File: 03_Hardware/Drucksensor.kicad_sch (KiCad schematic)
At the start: 100 parts, among them J110 DS18B20, J111 Conn_01x06_Male, Q1 BC817, SW103 SW_DIP_x08, U103 ATmega8A-A, U104 REF3040, U105 74HC165, U107 SN75176AD, U108 CAT24M01W, Y101 16MHz

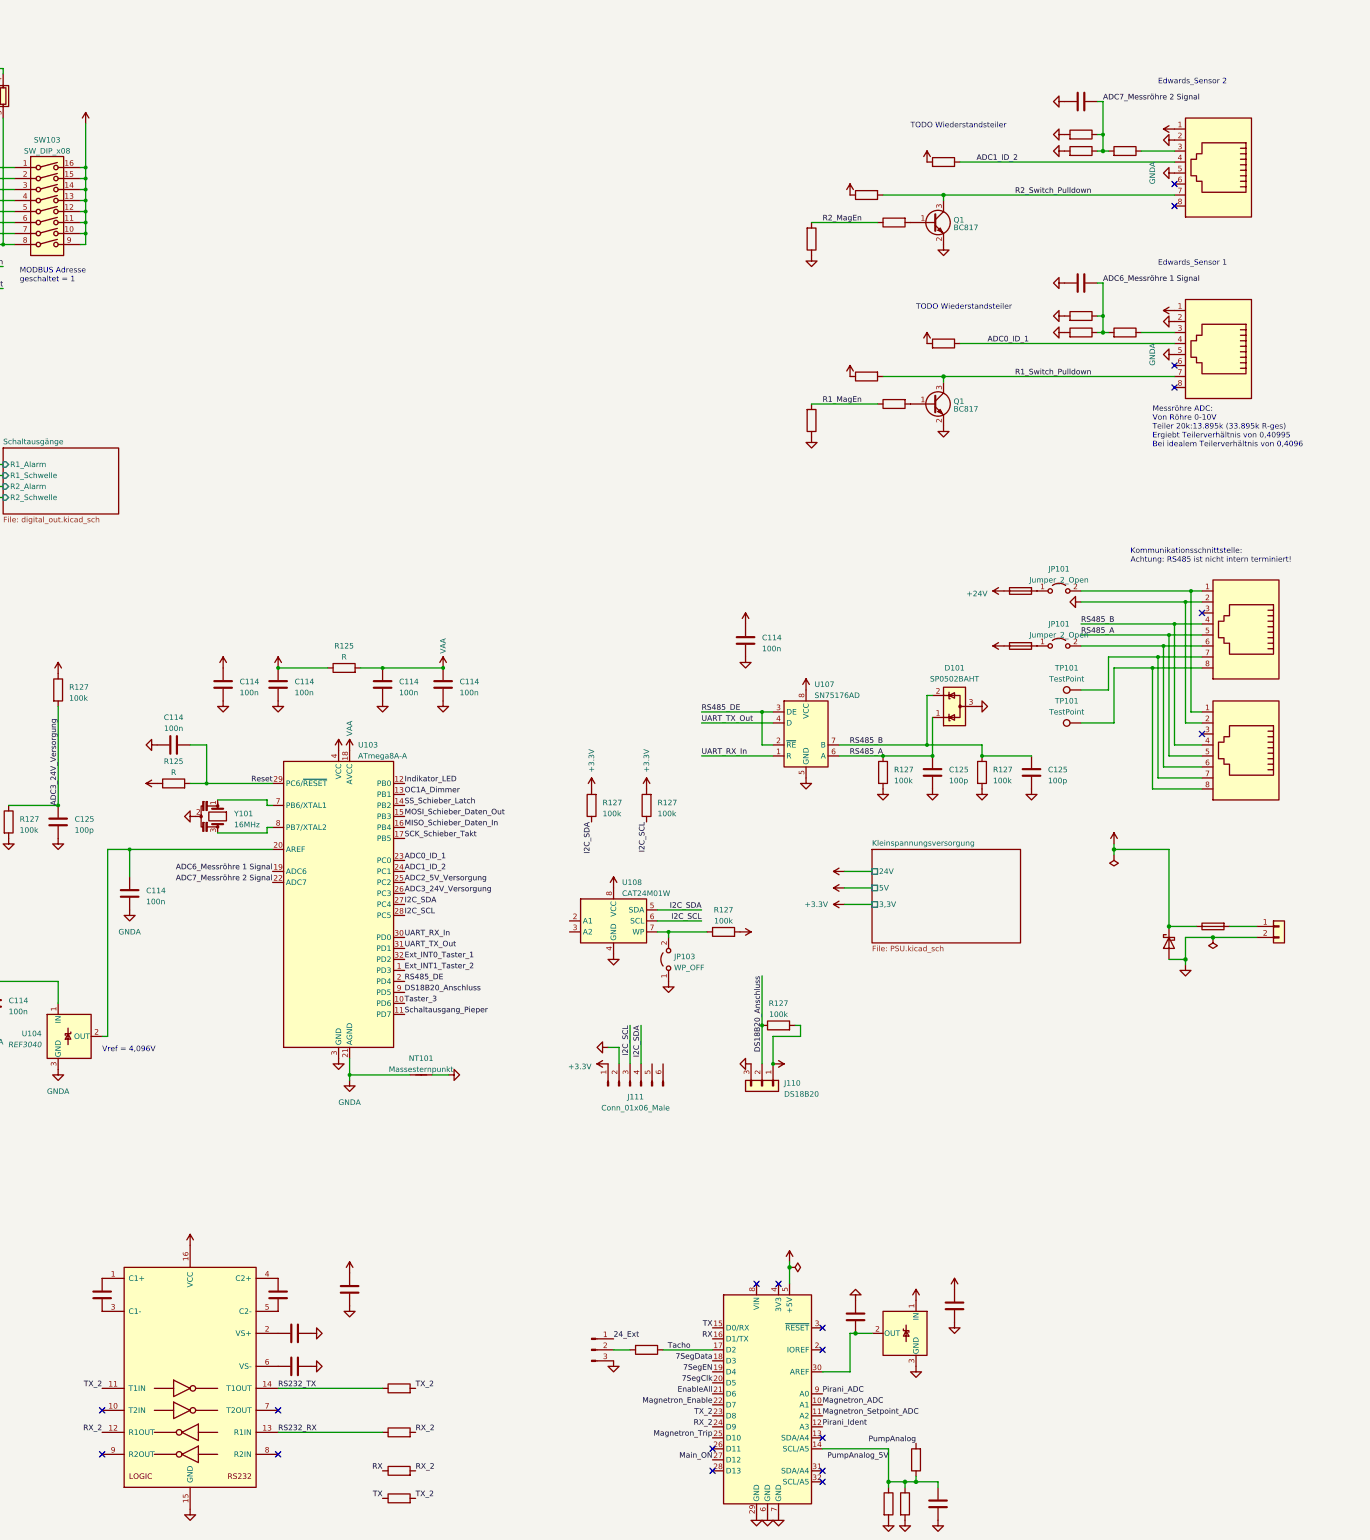
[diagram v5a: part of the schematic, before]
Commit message: RJ45-Anschlüsse überarbeitet
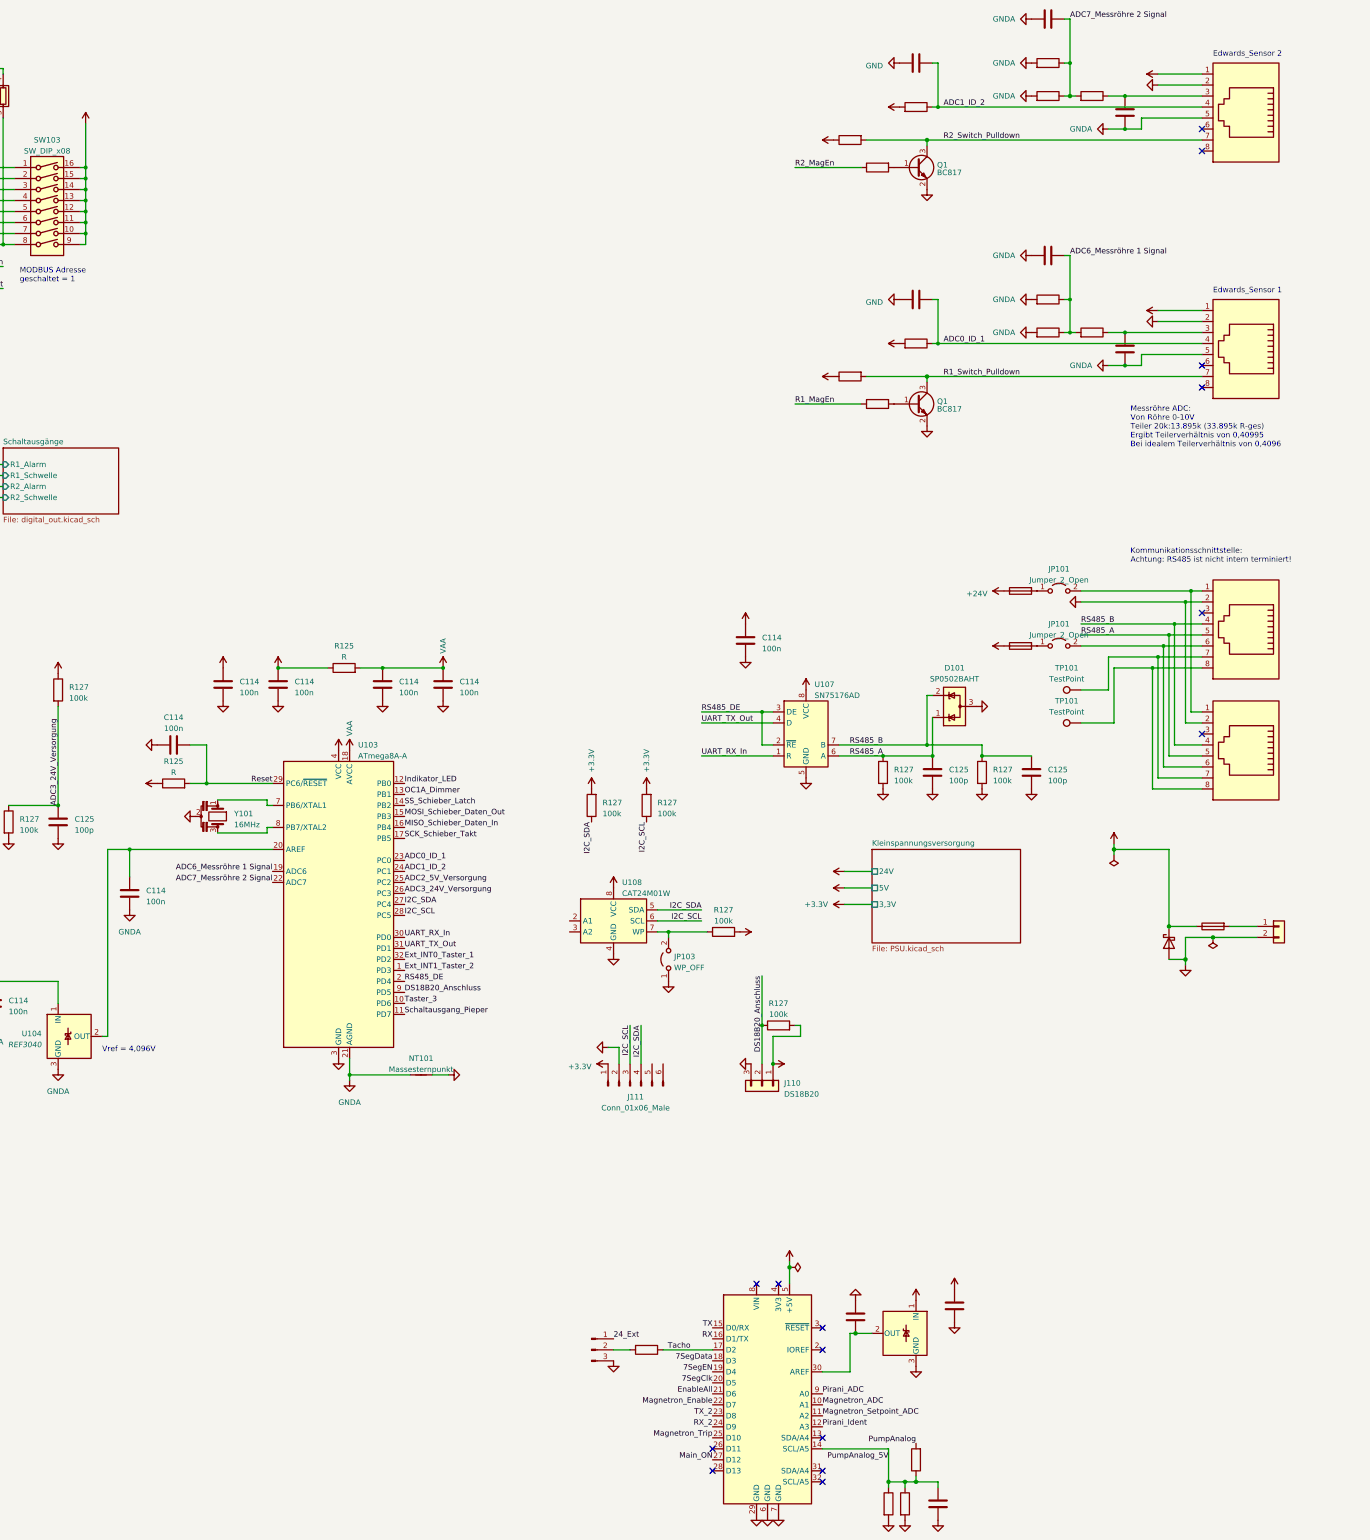
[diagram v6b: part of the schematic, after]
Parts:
- removed ? (x6): (no value), symbol Device:R
- removed ? (x5): (no value), symbol Device:C
- removed ?: (no value), symbol Interface_UART:MAX232
- added ? (x4): (no value), symbol Device:C
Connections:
- net ADC0_ID_1: now also ?.1
- net ADC1_ID_2: now also ?.1
- net GND: now also ?.2, ?.2; no longer ?.2, ?.2, ?.2, ?.2, ?.2, ?.2
- net GNDA: now also ?.2, ?.2, ?.2, ?.2, ?.2, ?.2, ?.2, ?.2
- net at ?.1, ?.3: now also ?.1 (x2)
- no-connect marks 23 -> 19
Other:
- note added: "Messröhre ADC: Von Röhre 0-10V Teiler 20k:13.895k (33.895k R-ges) Ergibt Teilerverhältnis von 0,40995 Bei idealem Teilerverhältnis von 0,4096"
- note removed: "Messröhre ADC: Von Röhre 0-10V Teiler 20k:13.895k (33.895k R-ges) Ergiebt Teilerverhältnis von 0,40995 Bei idealem Teilerverhältnis von 0,4096"
- note removed: "TODO Wiederstandsteiler"
- title: Vakkumanzeige für zwei aktive Vakuumsensoren -> Anzeigegerät für zwei aktive Vakuumsensoren
- moved on the sheet: Q1

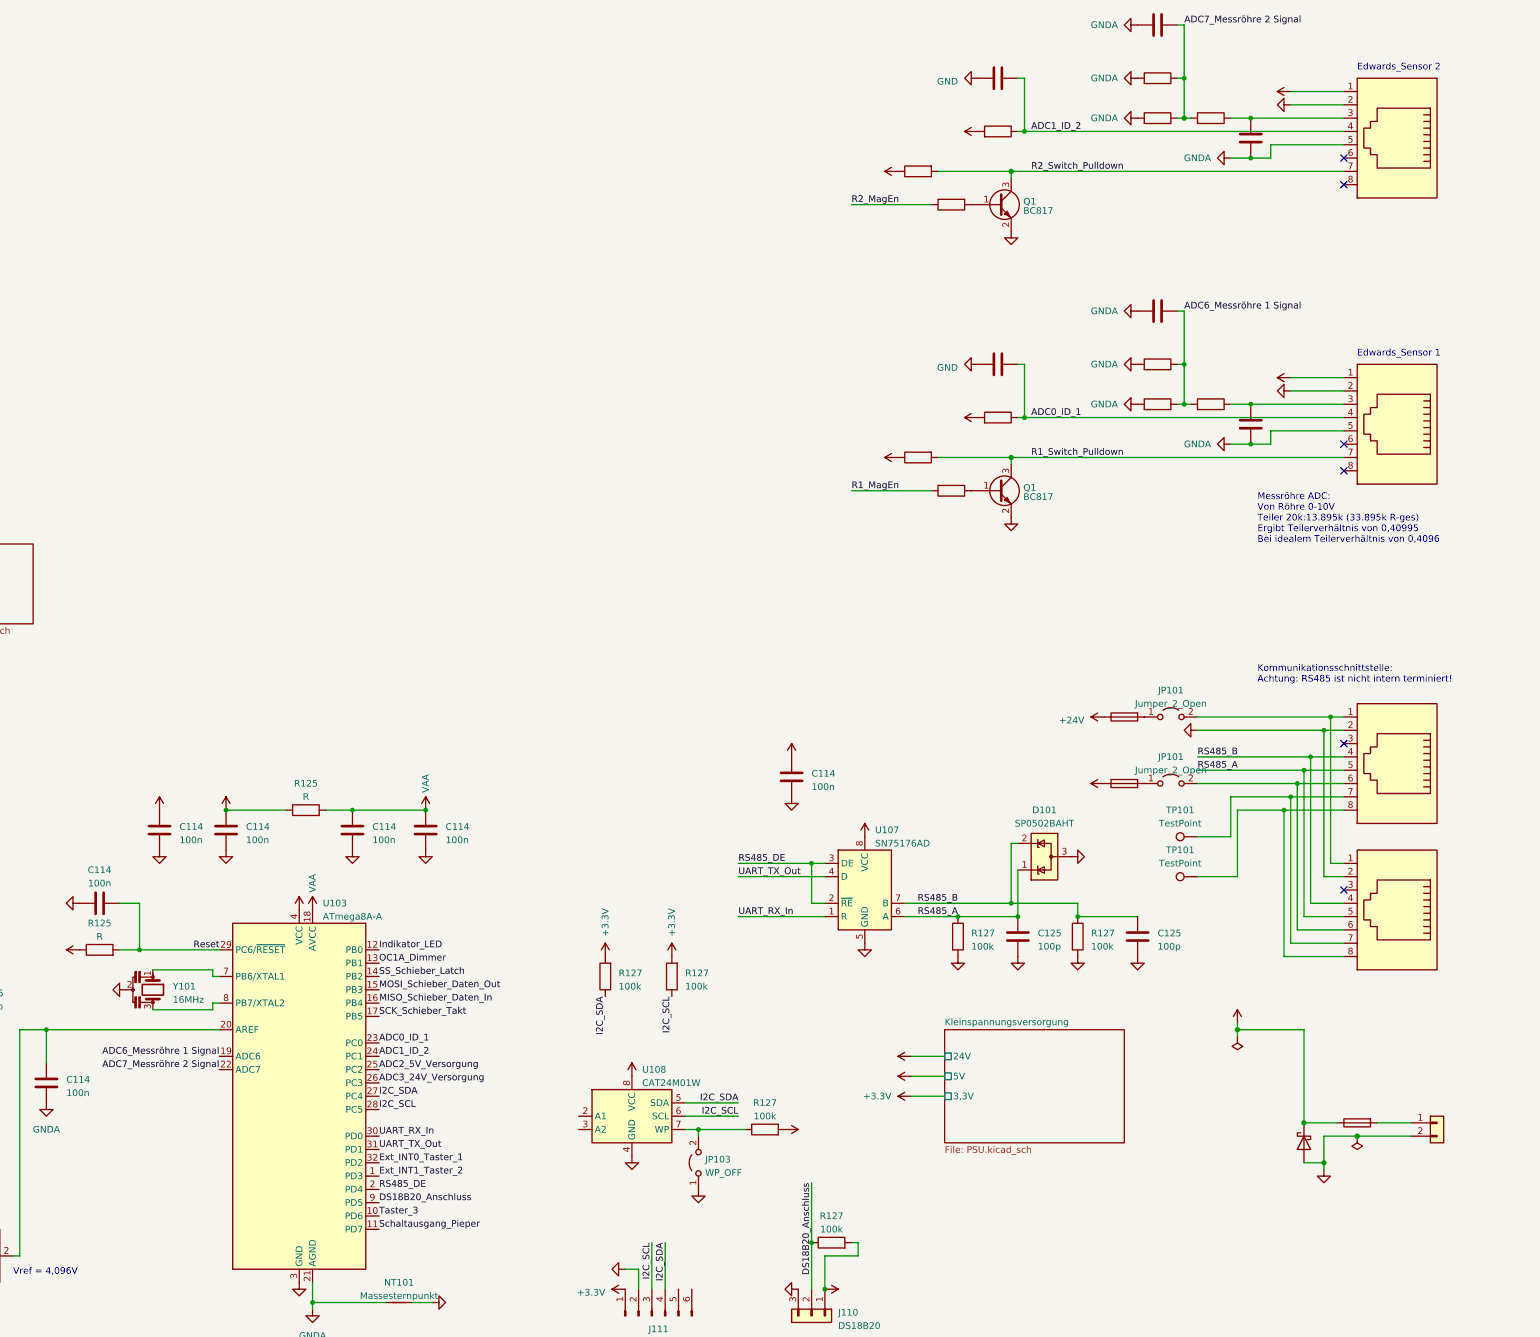
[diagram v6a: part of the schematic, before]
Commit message: TVS Dioden für Signal und DS18b20 hinzugefügt
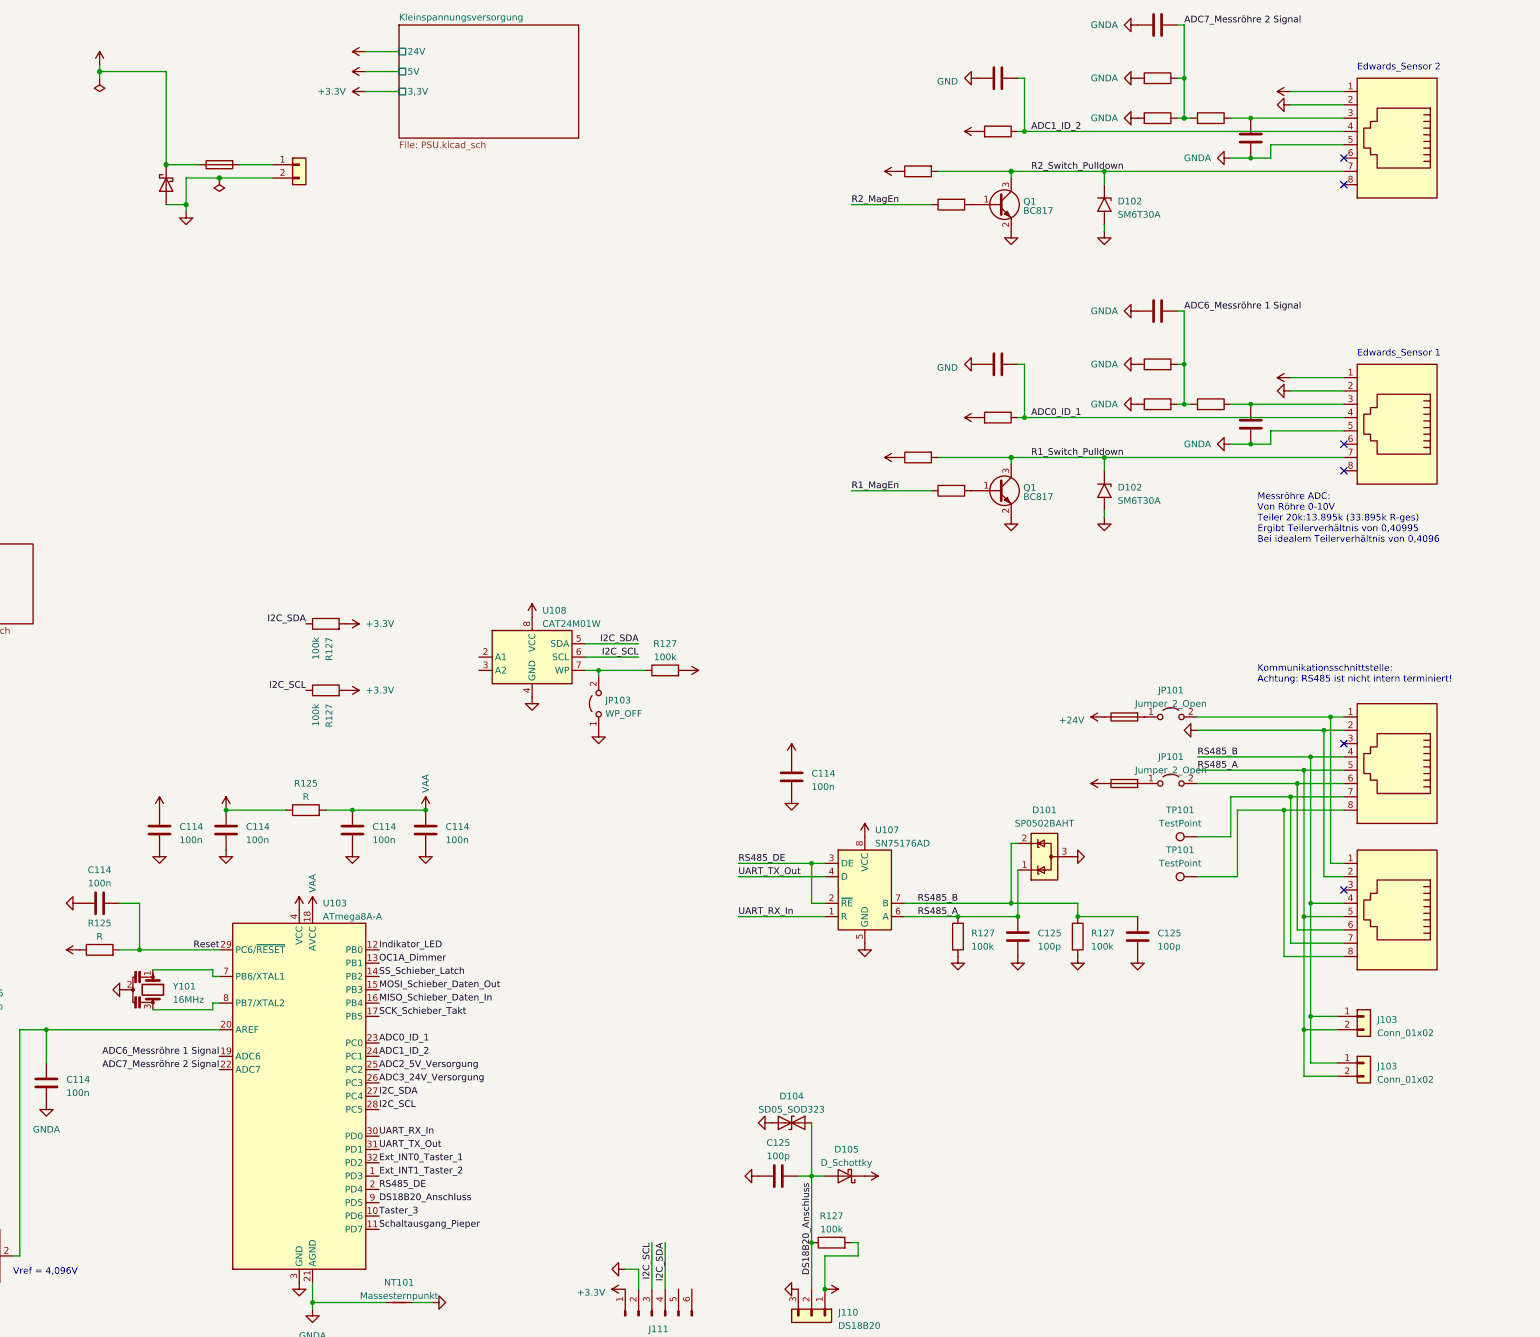
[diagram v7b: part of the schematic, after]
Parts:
- added C125: 100p, symbol Device:C
- added D102 (x2): SM6T30A, Diode_SMD:D_SMB, symbol Diode:SM6T30A
- added D104: SD05_SOD323, Diode_SMD:D_SOD-323, symbol Diode:SD05_SOD323
- added D105: D_Schottky, symbol Device:D_Schottky
- added J103 (x2): Conn_01x02, symbol Connector_Generic:Conn_01x02
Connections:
- net +5V: now also D105.1 (K)
- net DS18B20_Anschluss: now also C125.2, D104.2 (A2), D105.2 (A)
- net GND: now also C125.1, D102.2 (A2), D102.2 (A2), D104.1 (A1)
- net R1_Switch_Pulldown: now also D102.1 (A1)
- net R2_Switch_Pulldown: now also D102.1 (A1)
- net RS485_A: now also J103.2 (Pin_2), J103.2 (Pin_2)
- net RS485_B: now also J103.1 (Pin_1), J103.1 (Pin_1)
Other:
- moved on the sheet: JP103, R127, U108
